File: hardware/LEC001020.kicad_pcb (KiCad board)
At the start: 2 copper layers, 25 x 19 mm, 14 parts, among them J1 Screw_Terminal_01x02_blue

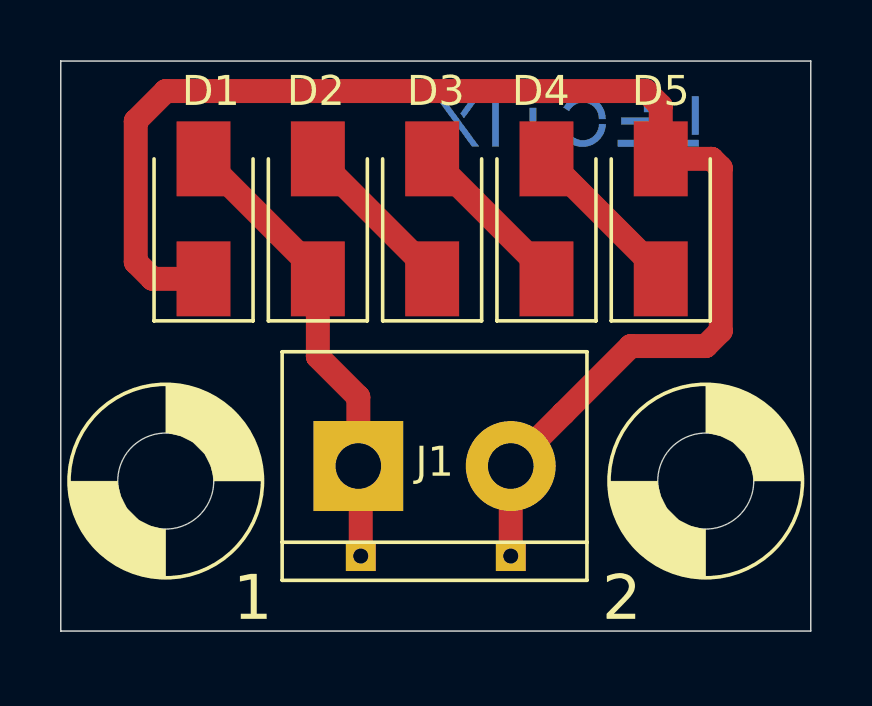
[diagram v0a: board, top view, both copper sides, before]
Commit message: Update schematic sheet settings + add open hardware logo
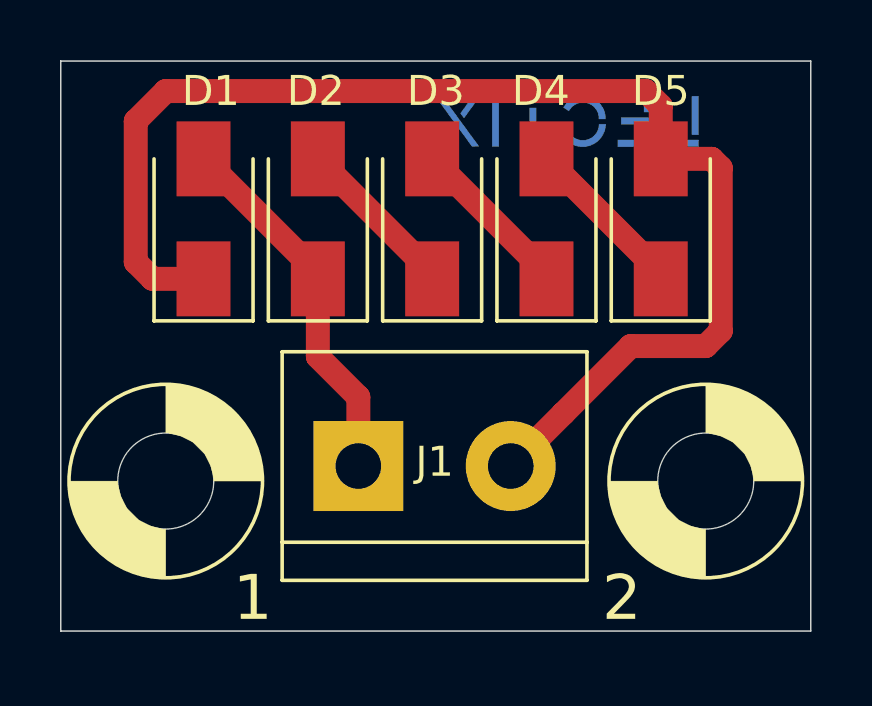
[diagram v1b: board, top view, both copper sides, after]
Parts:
- removed the REF** at (139.0, 80.5)
- removed TP1, TP2: TestPoint, TestPoint:TestPoint_THTPad_1.0x1.0mm_Drill0.5mm
- added REF**: OSHW-Logo2_7.3x6mm_SilkScreen, Symbol:OSHW-Logo2_7.3x6mm_SilkScreen, B.Cu at (138.2, 80.9)
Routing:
- net Net-(D1-Pad1): track 46.5 -> 43.5 mm
- net Net-(D1-Pad2): track 15.4 -> 12.5 mm
